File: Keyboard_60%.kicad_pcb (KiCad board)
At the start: 2 copper layers, 284.7 x 94.2 mm, 215 parts, among them J1 JST-4-pin, J3 Prog_conn, J4 TYPE-C-31-M12_13, J5 Tag connect TC2030-CTX, SW1 MK-12C02-G025, SW2 Reset Switch, U1 BQ24074RGTR, U3 nRF52840-QIAA-R/nRF52833-QIAA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, U4 TPD4E05U06DQAR, Y1 32MHz, Y2 32.768kHz

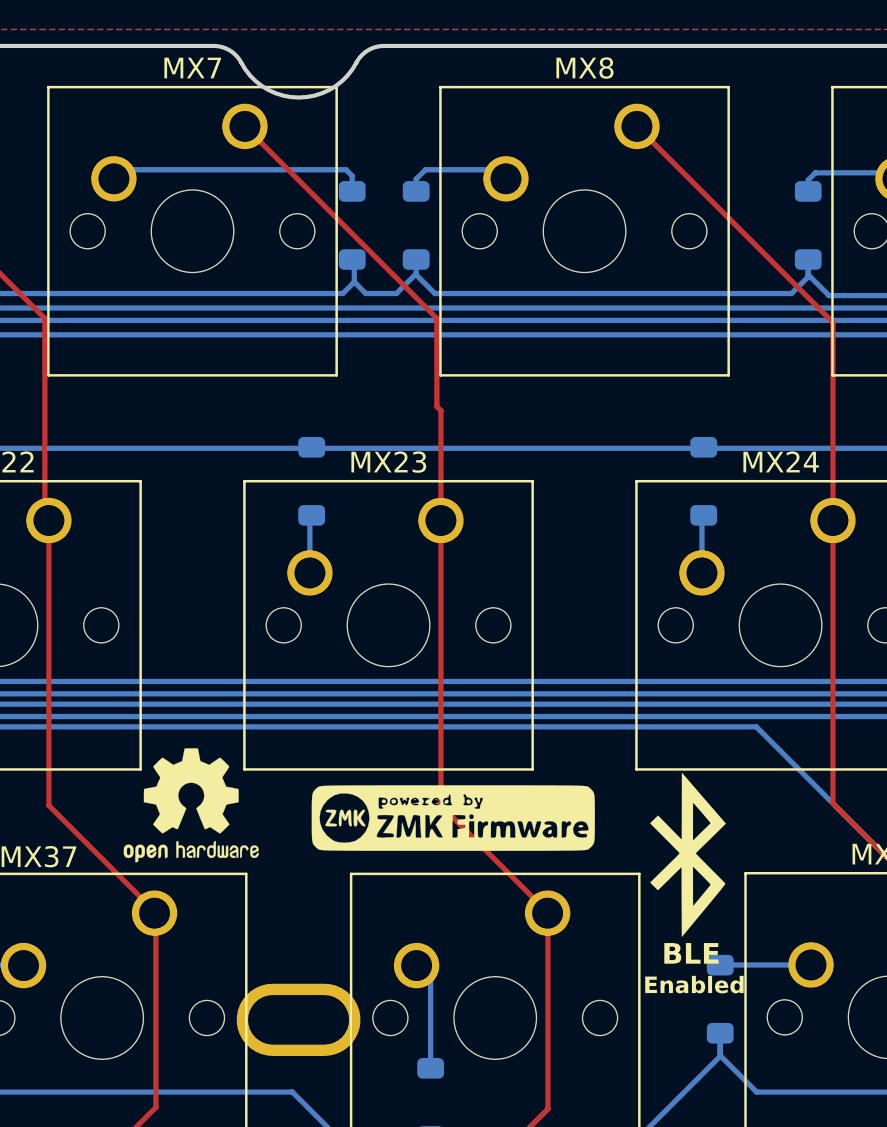
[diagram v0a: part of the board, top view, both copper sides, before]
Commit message: Changed the gerber to final production files
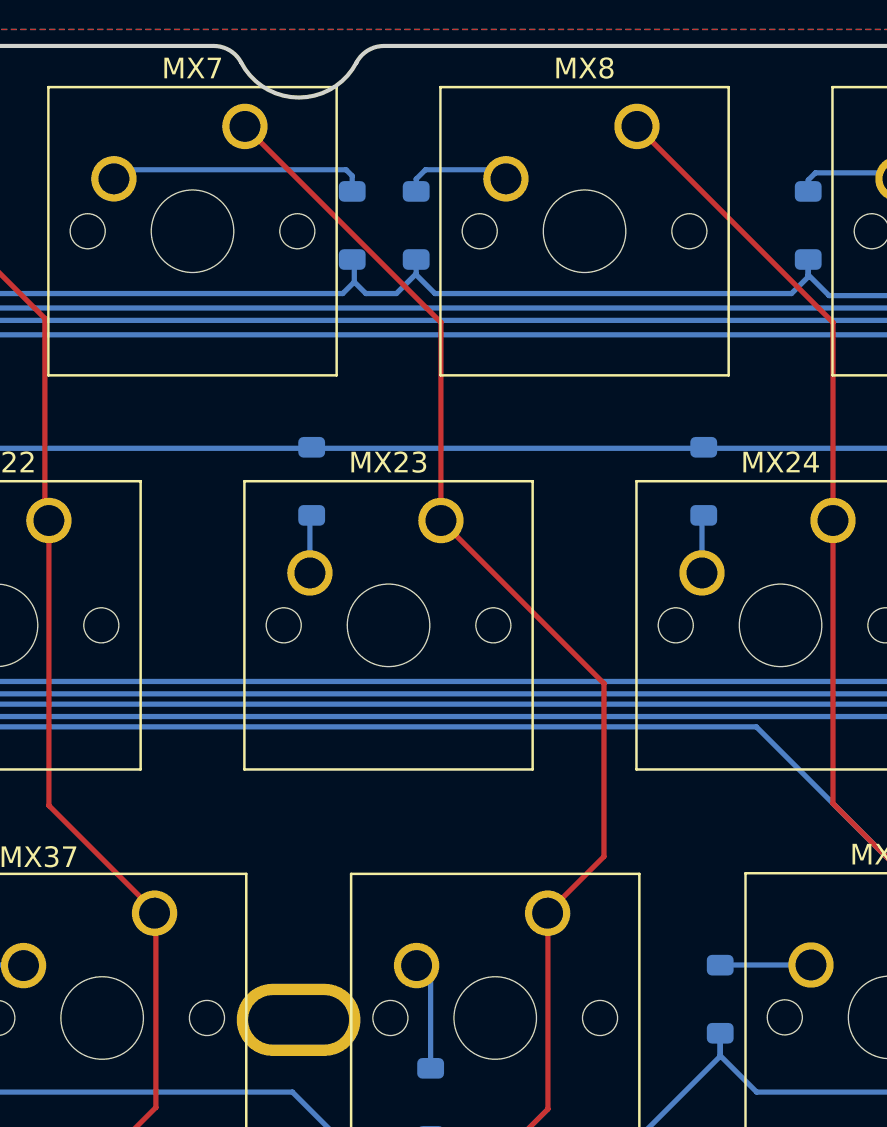
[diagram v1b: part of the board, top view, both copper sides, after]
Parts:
- removed the G*** at (165.0, 79.4)
- added G***: LOGO, keyboard:logo-soldermask, B.Cu at (165.7, 80.3)
- moved G*** 0.78 mm to (163.3, 89.1)
- moved REF** 0.36 mm to (123.7, 37.1)
- moved G*** 0.36 mm to (136.0, 38.3)
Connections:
- C10 pad 2: Net-(U3-VSS_PA) -> GND
- U3 pad F23: Net-(U3-VSS_PA) -> GND
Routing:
- net Net-(U3-VSS_PA): track 2.70 -> 0.00 mm
- net GND: track 24.1 -> 26.8 mm
- net /COL6: track 216.3 -> 218.6 mm
